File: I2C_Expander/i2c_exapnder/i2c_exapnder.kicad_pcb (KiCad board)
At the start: 2 copper layers, 60.9 x 50 mm, 8 parts, among them J1 Conn_01x10, J2 Conn_01x05, J3 Conn_01x05, J4 Conn_01x05

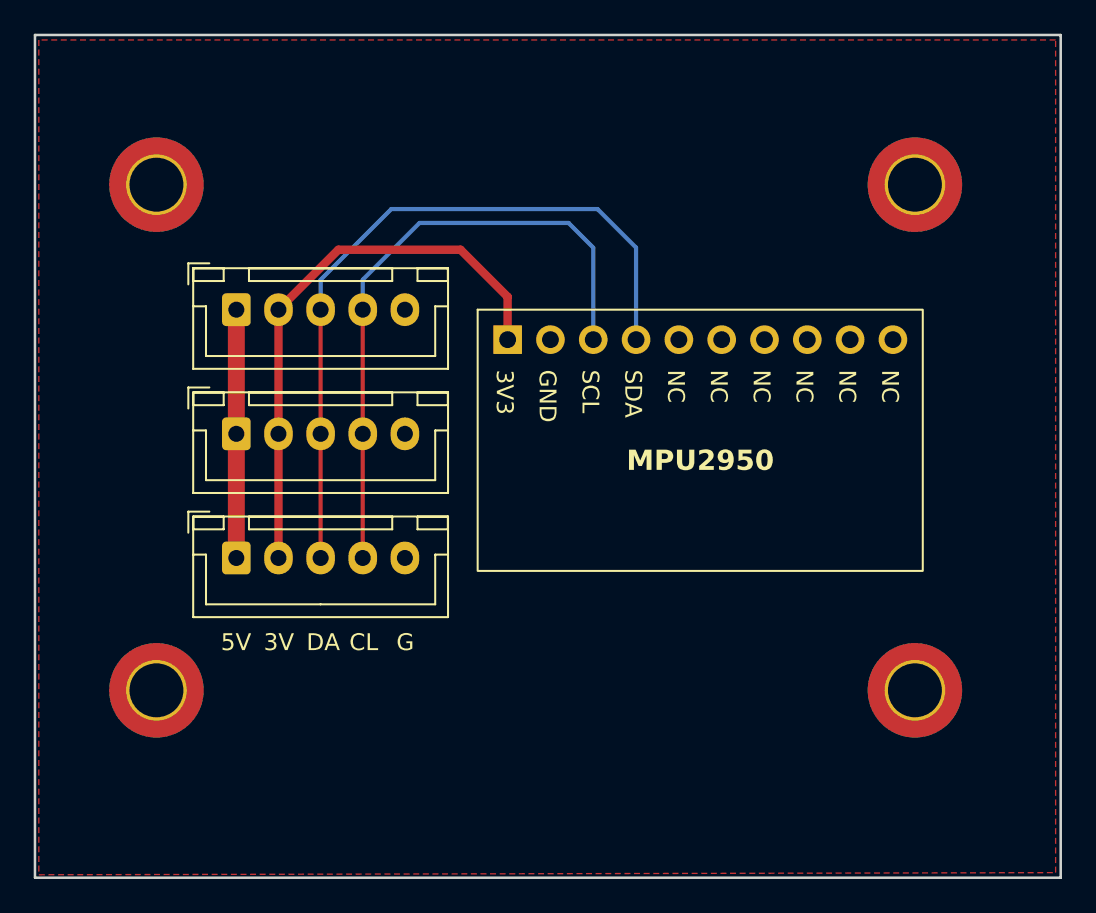
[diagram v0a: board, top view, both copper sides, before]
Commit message: Align I2C Expander screw holes
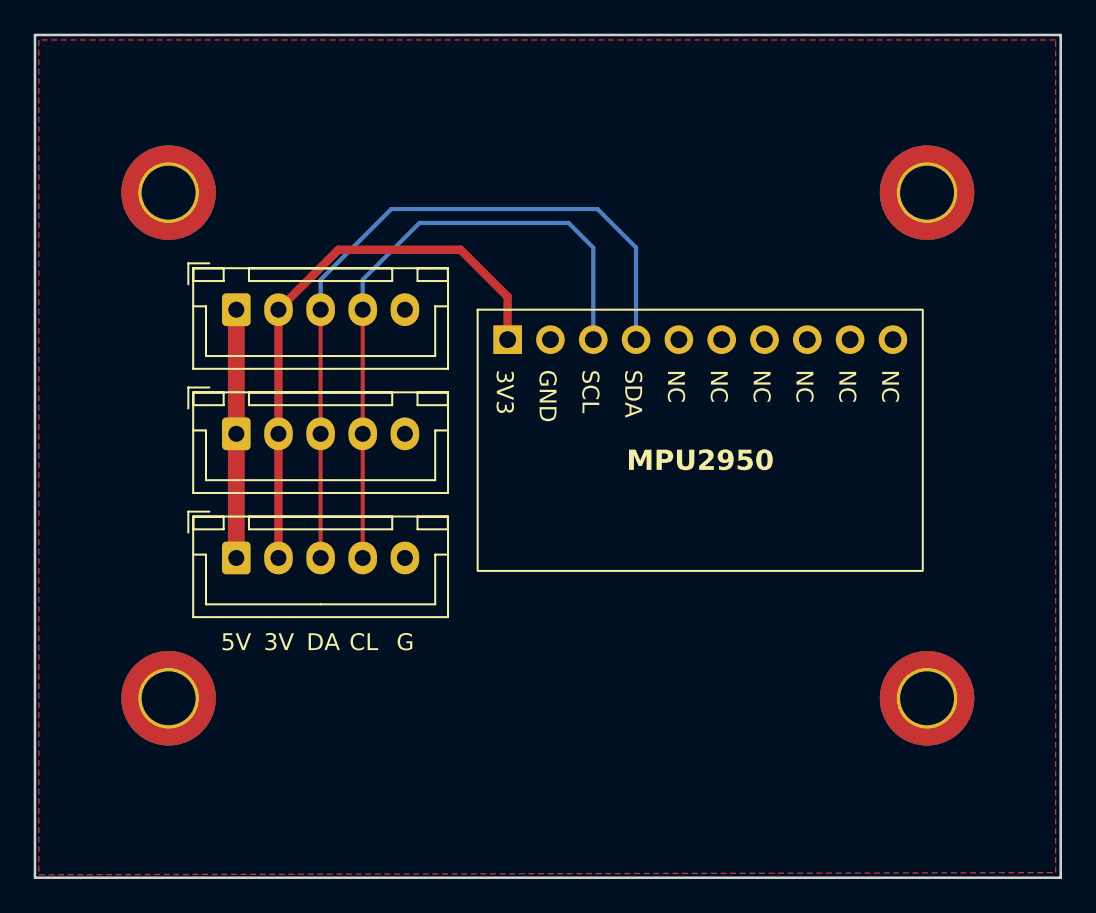
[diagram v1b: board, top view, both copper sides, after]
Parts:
- moved H1 0.86 mm to (128.2, 83.0)
- moved H2 0.86 mm to (173.2, 83.0)
- moved H3 0.86 mm to (128.2, 113.0)
- moved H4 0.86 mm to (173.2, 113.0)
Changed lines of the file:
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@@
   (net 11 "+5V")
   (footprint "MountingHole:MountingHole_3.2mm_M3_DIN965_Pad_TopBottom" (layer "F.Cu")
-    (at 172.5 112.5)
+    (at 173.221 112.97275)
     (descr "Mounting Hole 3.2mm, M3, DIN965")
     (tags "mounting hole 3.2mm m3 din965")
@@
   )
   (footprint "MountingHole:MountingHole_3.2mm_M3_DIN965_Pad_TopBottom" (layer "F.Cu")
-    (at 127.5 82.5)
+    (at 128.221 82.97275)
     (descr "Mounting Hole 3.2mm, M3, DIN965")
     (tags "mounting hole 3.2mm m3 din965")
@@
   )
   (footprint "MountingHole:MountingHole_3.2mm_M3_DIN965_Pad_TopBottom" (layer "F.Cu")
-    (at 172.5 82.5)
+    (at 173.221 82.97275)
     (descr "Mounting Hole 3.2mm, M3, DIN965")
     (tags "mounting hole 3.2mm m3 din965")
@@
   )
   (footprint "MountingHole:MountingHole_3.2mm_M3_DIN965_Pad_TopBottom" (layer "F.Cu")
-    (at 127.5 112.5)
+    (at 128.221 112.97275)
     (descr "Mounting Hole 3.2mm, M3, DIN965")
     (tags "mounting hole 3.2mm m3 din965")
@@
     )
   )
+  (group "" (id e18442a4-f133-432e-a6e6-ddf63e55b136)
+    (members
+      3fdd77ab-3c3b-44e2-b151-a674e002e698
+      b2849bb0-2dd7-4235-8b67-986864d79051
+      c14d7d9d-619c-4e12-959c-c906716fb7f4
+      eb1ab998-b369-4d68-9c0c-39bf390b0588
+    )
+  )
